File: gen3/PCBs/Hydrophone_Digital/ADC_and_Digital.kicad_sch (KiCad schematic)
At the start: 0 parts

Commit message: add ADC reference, clock and setup pins
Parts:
- added C1, C2, C3, C4, C9: 2.2u, Capacitor_SMD:C_0805_2012Metric_Pad1.18x1.45mm_HandSolder, symbol Device:C
- added C10: 100n, Capacitor_SMD:C_0805_2012Metric_Pad1.18x1.45mm_HandSolder, symbol Device:C
- added C5: 10u, Capacitor_SMD:C_0805_2012Metric_Pad1.18x1.45mm_HandSolder, symbol Device:C
- added C6, C7: 1u, Capacitor_SMD:C_0805_2012Metric_Pad1.18x1.45mm_HandSolder, symbol Device:C
- added C8: 22u, Capacitor_SMD:C_1206_3216Metric_Pad1.33x1.80mm_HandSolder, symbol Device:C
- added R1: 120k, Resistor_SMD:R_0805_2012Metric_Pad1.20x1.40mm_HandSolder, symbol Device:R
- added R2: 33, Resistor_SMD:R_0805_2012Metric_Pad1.20x1.40mm_HandSolder, symbol Device:R
- added R3, R4: 10k, Resistor_SMD:R_0805_2012Metric_Pad1.20x1.40mm_HandSolder, symbol Device:R
- added U1: ADS127L14IRSHR, robosub_footprints:IC_ADS127L14IRSHR, symbol robosub_symbols:ADS127L14IRSHR
- added U2: REF6041xDGK, Package_SO:VSSOP-8_3x3mm_P0.65mm, symbol Reference_Voltage:REF6041xDGK
- added Y1: 65.536MHz, Oscillator:Oscillator_SMD_ECS_2520MV-xxx-xx-4Pin_2.5x2.0mm, symbol Oscillator:ECS-2520MV-xxx-xx
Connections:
- new net: R2.1, Y1.3 (OUT)
- new net: R1.2, U2.3 (SS)
- new net: C6.2, U2.4 (FILT)
- new net +1V8: C10.1, C3.2, R3.2, U1.18 (IOVDD), U1.19 (IOVDD), U1.54 (MODE), Y1.1 (Tri-State), Y1.4 (VDD)
- new net +5VA: C1.2, C2.2, C7.1, R1.1, U1.23 (AVDD1), U1.24 (AVDD1), U1.25 (AVDD2), U2.1 (VIN), U2.2 (EN)
- new net ADC_CAPD: C4.2, U1.20 (CAPD)
- new net ADC_CLK: R2.2, U1.16 (CLKIN)
- new net ADC_ERROR_N: U1.5 (~{ERROR})
- new net ADC_REFP: C8.1, C9.1, U1.49 (REFP), U1.50 (REFP), U2.5 (OUT_S), U2.6 (OUT_F)
- new net ADC_RESET_N: R3.1, U1.52 (~{RESET})
- new net ADC_START: R4.1, U1.53 (START)
- new net AVSS: C1.1, C10.2, C2.1, C3.1, C4.1, C5.1, C6.1, C7.2, C8.2, C9.2, R4.2, U1.17 (DGND), U1.21 (DGND), U1.22 (AVSS), U1.28 (AVSS), U1.29 (AVSS), U1.30 (AVSS), U1.31 (AVSS), U1.32 (AVSS), U1.33 (AVSS), U1.34 (AVSS), U1.35 (AVSS), U1.36 (AVSS), U1.45 (AVSS), U1.47 (REFN), U1.48 (REFN), U1.51 (AVSS), U1.57 (THERMAL_PAD), U2.7 (GND_F), U2.8 (GND_S), Y1.2 (GND)
- new net CAPA: C5.2, U1.26 (CAPA), U1.27 (CAPA)
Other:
- note added: "ADC + decoupling"
- note added: "ADC control"
- note added: "clock"
- note added: "voltage reference"

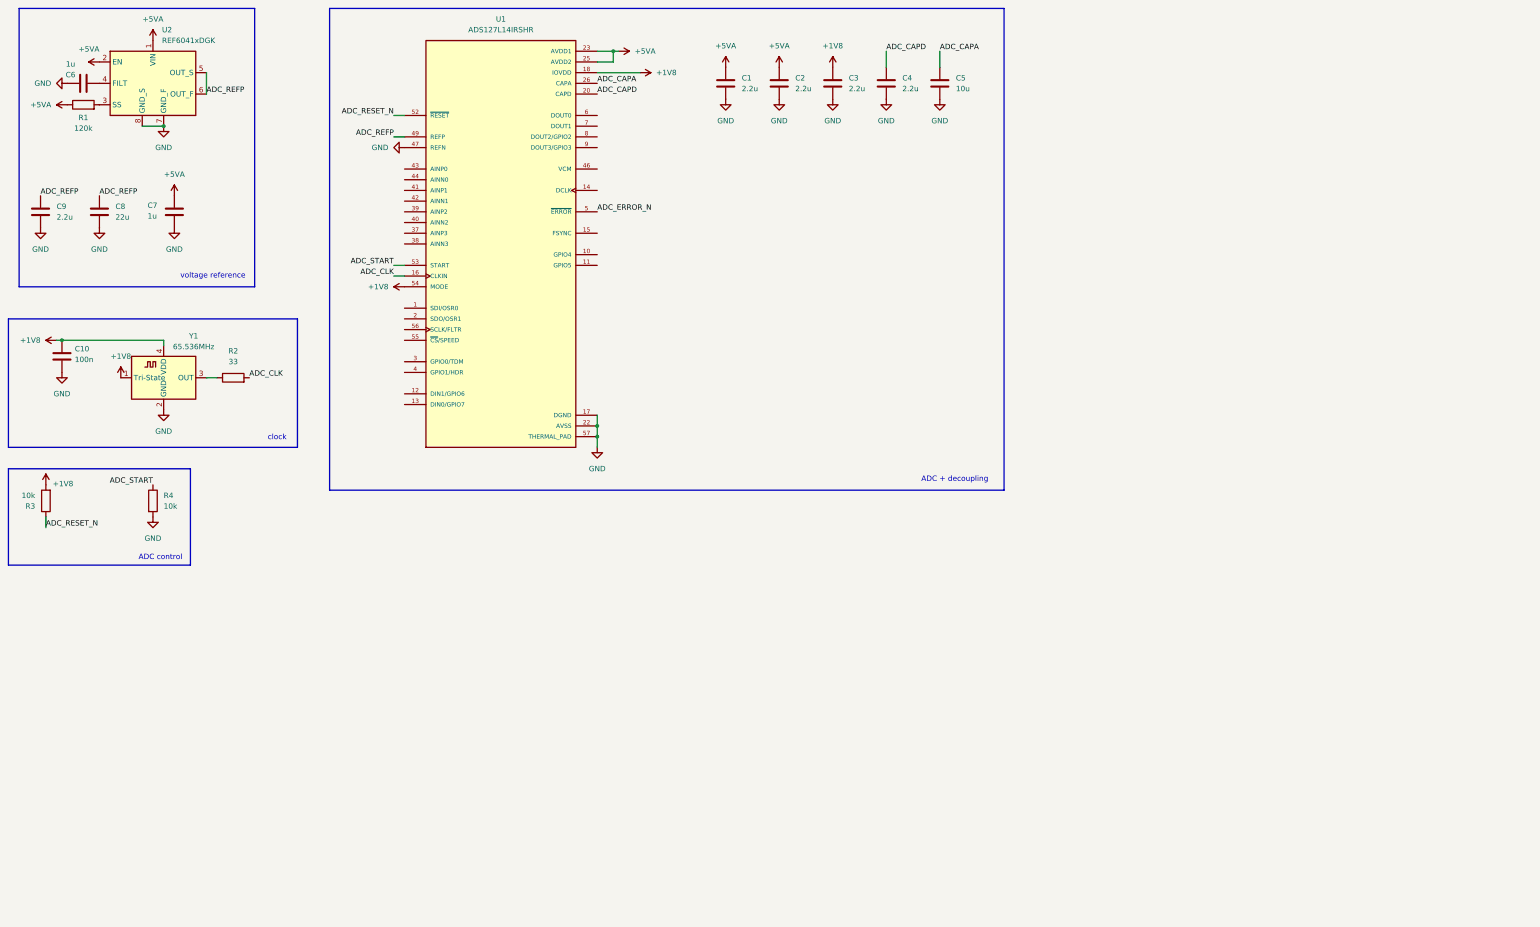
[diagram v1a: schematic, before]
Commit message: add 1.8v regulator, level shifters, microsd and daisy
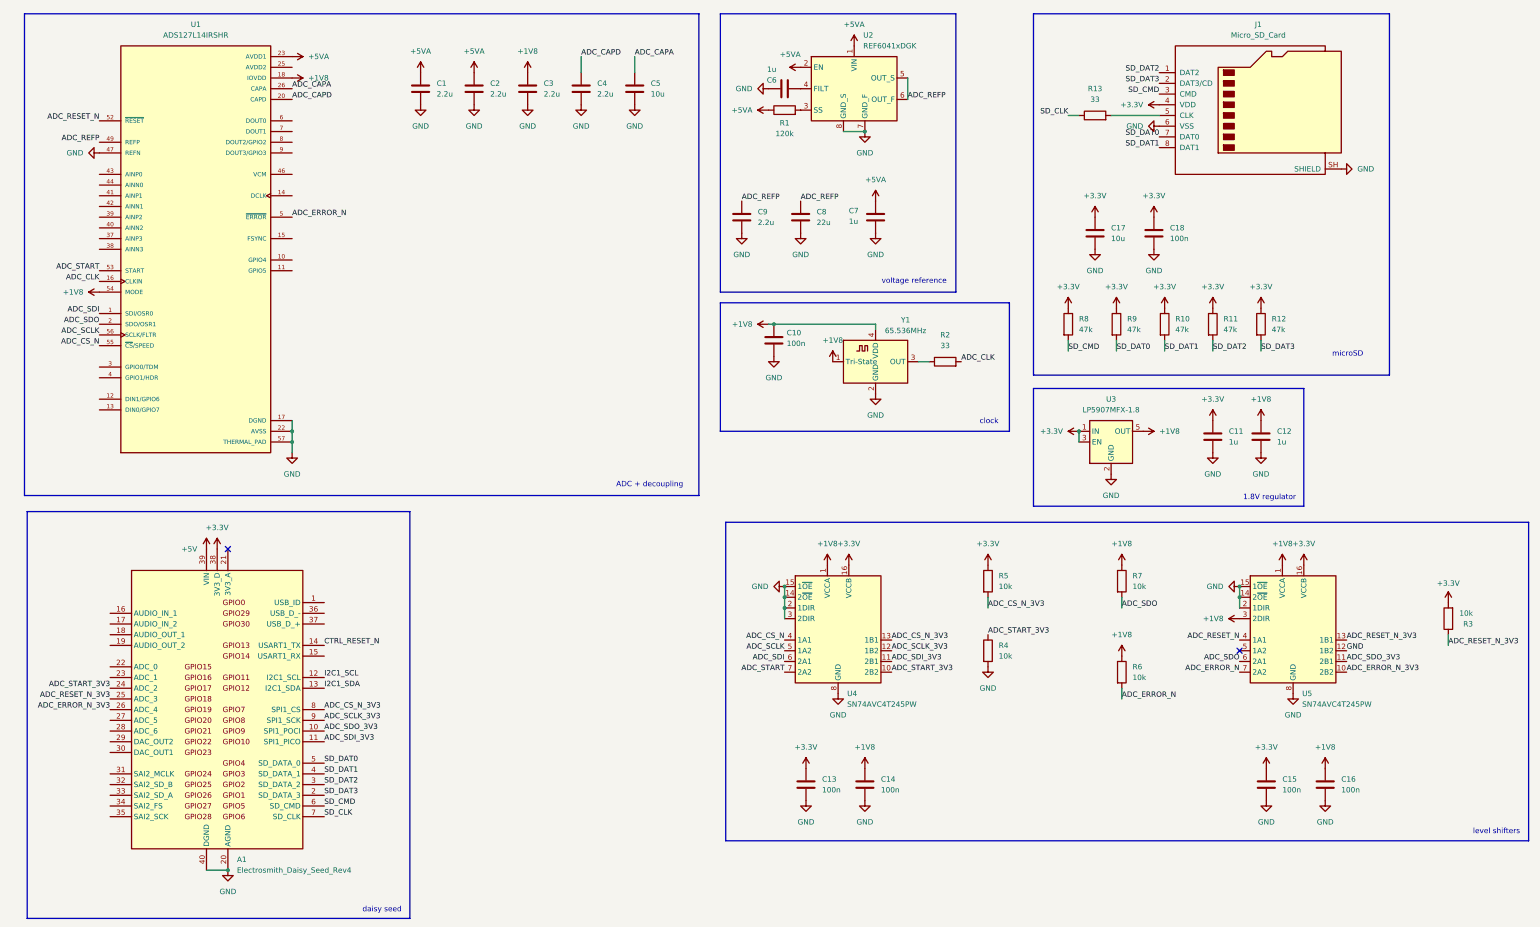
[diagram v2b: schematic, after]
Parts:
- added A1: Electrosmith_Daisy_Seed_Rev4, Module:Electrosmith_Daisy_Seed, symbol MCU_Module:Electrosmith_Daisy_Seed_Rev4
- added C11, C12: 1u, Capacitor_SMD:C_0805_2012Metric_Pad1.18x1.45mm_HandSolder, symbol Device:C
- added C13, C14, C15, C16, C18: 100n, Capacitor_SMD:C_0805_2012Metric_Pad1.18x1.45mm_HandSolder, symbol Device:C
- added C17: 10u, Capacitor_SMD:C_0805_2012Metric_Pad1.18x1.45mm_HandSolder, symbol Device:C
- added J1: Micro_SD_Card, Connector_Card:microSD_HC_Molex_104031-0811, symbol Connector:Micro_SD_Card
- added R10, R11, R12, R8, R9: 47k, Resistor_SMD:R_0805_2012Metric_Pad1.20x1.40mm_HandSolder, symbol Device:R
- added R13: 33, Resistor_SMD:R_0805_2012Metric_Pad1.20x1.40mm_HandSolder, symbol Device:R
- added R5, R6, R7: 10k, Resistor_SMD:R_0805_2012Metric_Pad1.20x1.40mm_HandSolder, symbol Device:R
- added U3: LP5907MFX-1.8, Package_TO_SOT_SMD:SOT-23-5, symbol Regulator_Linear:LP5907MFX-1.8
- added U4, U5: SN74AVC4T245PW, Package_SO:TSSOP-16_4.4x5mm_P0.65mm, symbol Logic_LevelTranslator:SN74AVC4T245PW
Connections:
- net +1V8: now also C12.1, C14.1, C16.1, R6.1, R7.1, U3.5 (OUT), U4.1 (VCCA), U5.1 (VCCA), U5.3 (2DIR); no longer R3.2
- net +5VA: no longer U1.25 (AVDD2)
- net ADC_ERROR_N: now also R6.2, U5.7 (2A2)
- net ADC_RESET_N: now also U5.4 (1A1); no longer R3.1
- net ADC_START: now also U4.7 (2A2); no longer R4.1
- net AVSS: now also A1.20 (AGND), A1.40 (DGND), C11.2, C12.2, C13.2, C14.2, C15.2, C16.2, C17.2, C18.2, J1.6 (VSS), J1.SH (SHIELD), U3.2 (GND), U4.14 (2~{OE}), U4.15 (1~{OE}), U4.2 (1DIR), U4.3 (2DIR), U4.8 (GND), U4.9 (GND), U5.12 (1B2), U5.14 (2~{OE}), U5.15 (1~{OE}), U5.2 (1DIR), U5.8 (GND), U5.9 (GND)
- net ADC_SDI: now reaches U1.1 (SDI/OSR0)
- net ADC_SDI: now also U4.6 (2A1)
- net ADC_SDO: now reaches U1.2 (SDO/OSR1)
- net ADC_SDO: now also R7.2, U5.6 (2A1)
- net ADC_CS_N: now reaches U1.55 (~{CS}/SPEED)
- net ADC_CS_N: now also U4.4 (1A1)
- net ADC_SCLK: now reaches U1.56 (SCLK/FLTR)
- net ADC_SCLK: now also U4.5 (1A2)
- new net: J1.5 (CLK), R13.2
- new net +3.3V: A1.38 (3V3_D), C11.1, C13.1, C15.1, C17.1, C18.1, J1.4 (VDD), R10.1, R11.1, R12.1, R3.2, R5.1, R8.1, R9.1, U3.1 (IN), U3.3 (EN), U4.16 (VCCB), U5.16 (VCCB)
- new net +5V: A1.39 (VIN)
- new net ADC_CS_N_3V3: A1.8 (SPI1_CS), R5.2, U4.13 (1B1)
- new net ADC_ERROR_N_3V3: A1.26 (ADC_4), U5.10 (2B2)
- new net ADC_RESET_N_3V3: A1.25 (ADC_3), R3.1, U5.13 (1B1)
- new net ADC_SCLK_3V3: A1.9 (SPI1_SCK), U4.12 (1B2)
- new net ADC_SDI_3V3: A1.11 (SPI1_PICO), U4.11 (2B1)
- new net ADC_SDO_3V3: A1.10 (SPI1_POCI), U5.11 (2B1)
- new net ADC_START_3V3: A1.24 (ADC_2), R4.1, U4.10 (2B2)
- new net CTRL_RESET_N: A1.14 (USART1_TX)
- new net I2C1_SCL: A1.12 (I2C1_SCL)
- new net I2C1_SDA: A1.13 (I2C1_SDA)
- new net SD_CLK: A1.7 (SD_CLK), R13.1
- new net SD_CMD: A1.6 (SD_CMD), J1.3 (CMD), R8.2
- new net SD_DAT0: A1.5 (SD_DATA_0), J1.7 (DAT0), R9.2
- new net SD_DAT1: A1.4 (SD_DATA_1), J1.8 (DAT1), R10.2
- new net SD_DAT2: A1.3 (SD_DATA_2), J1.1 (DAT2), R11.2
- new net SD_DAT3: A1.2 (SD_DATA_3), J1.2 (DAT3/CD), R12.2
- no-connect marks 0 -> 2
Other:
- note added: "1.8V regulator"
- note added: "daisy seed"
- note added: "level shifters"
- note added: "microSD"
- note removed: "ADC control"
- moved on the sheet: C1, C10, C2, C3, C4, C5, C6, C7, C8, C9, R1, R2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
